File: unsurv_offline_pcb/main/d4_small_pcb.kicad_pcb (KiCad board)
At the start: 4 copper layers, 32 x 45 mm, 61 parts, among them J1 U_FL-R-SMT-1_10_, J2 S2B-PH-SM4-TB_LF__SN_, Q1 UMH3N, U1 TTGO-Micro32-ESP32, U2 RF430CL330HIRGTR‎, U3 CAM-M8C-0-10, U4 AP2112K-3.3, U5 CH340G, U6 BQ25180, U7 BMA400-I2C, U8 RFM95W-868S2

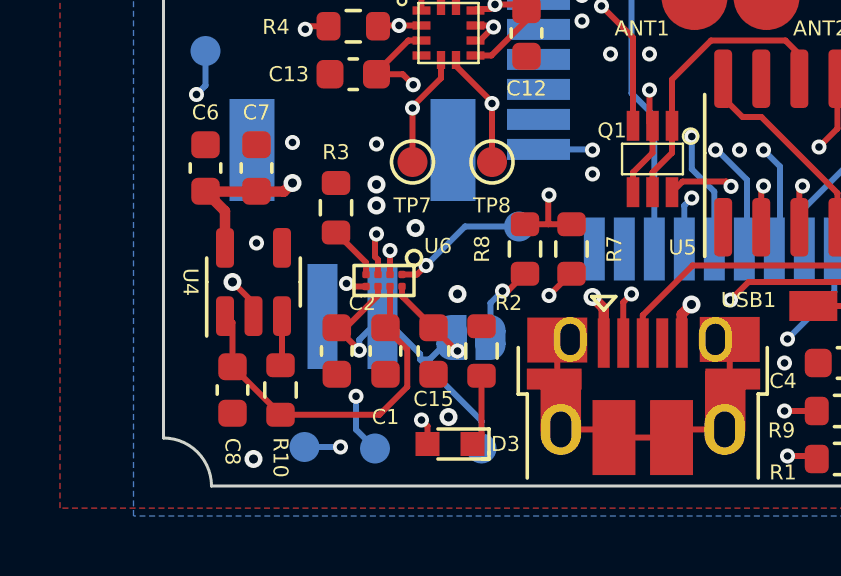
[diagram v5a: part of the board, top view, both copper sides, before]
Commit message: lower clearance for GND fills
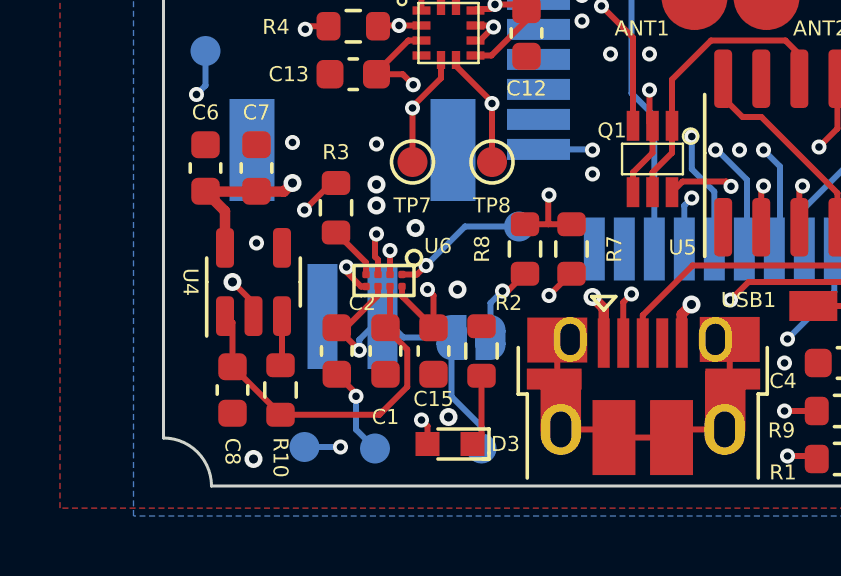
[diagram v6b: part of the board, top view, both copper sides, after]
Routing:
- net GND: track 16.9 -> 19.6 mm, vias 74 -> 75
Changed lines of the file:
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@@
   (segment (start 25.15 58.35) (end 25.15 58.65) (width 0.2) (layer "F.Cu") (net 3))
   (via (at 24.526334 60.475) (size 0.5) (drill 0.25) (layers "F.Cu" "B.Cu") (net 3))
-  (segment (start 26.867721 60.782279) (end 27.6 60.05) (width 0.2) (layer "B.Cu") (net 3))
-  (segment (start 28.6 63.75) (end 28.6 62.827668) (width 0.2) (layer "B.Cu") (net 3))
   (segment (start 24.526334 60.475) (end 24.526334 60.123666) (width 0.2) (layer "B.Cu") (net 3))
   (segment (start 24.526334 60.123666) (end 25.3 59.35) (width 0.2) (layer "B.Cu") (net 3))
-  (segment (start 26.554611 60.782279) (end 26.554611 60.604611) (width 0.2) (layer "B.Cu") (net 3))
-  (segment (start 26.554611 60.782279) (end 26.867721 60.782279) (width 0.2) (layer "B.Cu") (net 3))
-  (segment (start 26.554611 60.604611) (end 25.3 59.35) (width 0.2) (layer "B.Cu") (net 3))
-  (segment (start 28.6 62.827668) (end 26.554611 60.782279) (width 0.2) (layer "B.Cu") (net 3))
+  (segment (start 28.6 63.75) (end 28.6 63.022182) (width 0.2) (layer "B.Cu") (net 3))
+  (segment (start 27.6 60.05) (end 26 60.05) (width 0.2) (layer "B.Cu") (net 3))
+  (segment (start 27.6 62.022182) (end 27.6 60.05) (width 0.2) (layer "B.Cu") (net 3))
+  (segment (start 26 60.05) (end 25.3 59.35) (width 0.2) (layer "B.Cu") (net 3))
+  (segment (start 28.6 63.022182) (end 27.6 62.022182) (width 0.2) (layer "B.Cu") (net 3))
+  (segment (start 24.417052 61.915718) (end 23.776334 61.275) (width 0.2) (layer "F.Cu") (net 4))
   (segment (start 39.7 39.75) (end 39.7 39.056416) (width 0.2) (layer "F.Cu") (net 4))
   (segment (start 31.575 57.925) (end 30.85 58.65) (width 0.2) (layer "F.Cu") (net 4))
+  (segment (start 24.1 57.7) (end 24.1 57.866942) (width 0.2) (layer "F.Cu") (net 4))
   (segment (start 26.6 49.15) (end 26.6 48.5) (width 0.2) (layer "F.Cu") (net 4))
   (segment (start 39 39.05) (end 39.706416 39.05) (width 0.2) (layer "F.Cu") (net 4))
+  (segment (start 23.6 54.9) (end 22.7 55.8) (width 0.2) (layer "F.Cu") (net 4))
   (segment (start 35.9 39.75) (end 36.8 39.75) (width 0.2) (layer "F.Cu") (net 4))
   (segment (start 39.706416 39.05) (end 40.05 39.05) (width 0.2) (layer "F.Cu") (net 4))
+  (segment (start 23.75 54.9) (end 23.6 54.9) (width 0.2) (layer "F.Cu") (net 4))
   (segment (start 35.6 58.949989) (end 35.275 59.274989) (width 0.35) (layer "F.Cu") (net 4))
   (segment (start 40.05 39.05) (end 40.65 38.45) (width 0.2) (layer "F.Cu") (net 4))
@@
   (segment (start 40.65 37.75) (end 39.1 36.2) (width 0.2) (layer "F.Cu") (net 4))
   (segment (start 21 58.9) (end 21 59.3) (width 0.2) (layer "F.Cu") (net 4))
-  (segment (start 24.2 58.35) (end 24.75 58.35) (width 0.2) (layer "F.Cu") (net 4))
   (segment (start 33.25 39.25) (end 33.5875 39.5875) (width 0.2) (layer "F.Cu") (net 4))
-  (segment (start 24.1 58.25) (end 24.2 58.35) (width 0.2) (layer "F.Cu") (net 4))
   (segment (start 29 49.7) (end 28.55 50.15) (width 0.2) (layer "F.Cu") (net 4))
   (segment (start 20.3 58.2) (end 21 58.9) (width 0.2) (layer "F.Cu") (net 4))
@@
   (segment (start 28.55 50.15) (end 28.4 50.15) (width 0.2) (layer "F.Cu") (net 4))
   (segment (start 35.275 59.274989) (end 35.275 60.235) (width 0.35) (layer "F.Cu") (net 4))
+  (segment (start 24.583058 58.35) (end 24.75 58.35) (width 0.2) (layer "F.Cu") (net 4))
   (segment (start 29 49.7) (end 28.95 49.65) (width 0.2) (layer "F.Cu") (net 4))
+  (segment (start 24.1 57.866942) (end 24.583058 58.35) (width 0.2) (layer "F.Cu") (net 4))
+  (segment (start 24.417052 62.009055) (end 24.417052 61.915718) (width 0.2) (layer "F.Cu") (net 4))
   (via (at 46 60.1) (size 0.5) (drill 0.25) (layers "F.Cu" "B.Cu") (net 4))
   (via (at 39.9 46.9) (size 0.5) (drill 0.25) (layers "F.Cu" "B.Cu") (net 4))
@@
   (via (at 48.5 23.9) (size 0.5) (drill 0.25) (layers "F.Cu" "B.Cu") (net 4))
   (via (at 19.4 30.4) (size 0.5) (drill 0.25) (layers "F.Cu" "B.Cu") (net 4))
+  (via (at 22.7 55.8) (size 0.5) (drill 0.25) (layers "F.Cu" "B.Cu") (net 4))
   (via (at 44.1 32.7) (size 0.5) (drill 0.25) (layers "F.Cu" "B.Cu") (net 4))
   (via (at 27.5 30.4) (size 0.5) (drill 0.25) (layers "F.Cu" "B.Cu") (net 4))
@@
   (via (at 35.5 30.4) (size 0.5) (drill 0.25) (layers "F.Cu" "B.Cu") (net 4))
   (via (at 35.1 23.2) (size 0.5) (drill 0.25) (layers "F.Cu" "B.Cu") (net 4))
-  (via (at 24.1 58.25) (size 0.5) (drill 0.25) (layers "F.Cu" "B.Cu") (net 4))
+  (via (at 24.1 57.7) (size 0.5) (drill 0.25) (layers "F.Cu" "B.Cu") (net 4))
   (via (at 29 49.7) (size 0.5) (drill 0.25) (layers "F.Cu" "B.Cu") (net 4))
   (via (at 21.5 30.7) (size 0.5) (drill 0.25) (layers "F.Cu" "B.Cu") (net 4))
@@
   (via (at 44 29.5) (size 0.5) (drill 0.25) (layers "F.Cu" "B.Cu") (net 4))
   (via (at 27.5 42.4) (size 0.5) (drill 0.25) (layers "F.Cu" "B.Cu") (net 4))
-  (via (at 27.8 58.6) (size 0.6) (drill 0.3) (layers "F.Cu" "B.Cu") (net 4))
+  (via (at 27.8 58.45) (size 0.6) (drill 0.3) (layers "F.Cu" "B.Cu") (net 4))
   (via (at 44.1 23.3) (size 0.5) (drill 0.25) (layers "F.Cu" "B.Cu") (net 4))
   (via (at 35.4 39.25) (size 0.5) (drill 0.25) (layers "F.Cu" "B.Cu") (net 4))
@@
   (segment (start 26.8 63) (end 26.6 62.8) (width 0.2) (layer "F.Cu") (net 5))
   (segment (start 32.3 58.7) (end 32.675 59.075) (width 0.35) (layer "F.Cu") (net 5))
-  (segment (start 27.775 60.5) (end 27 59.725) (width 0.2) (layer "F.Cu") (net 5))
-  (segment (start 27.8 60.5) (end 27.775 60.5) (width 0.2) (layer "F.Cu") (net 5))
+  (segment (start 27 58.65) (end 27 59.725) (width 0.2) (layer "F.Cu") (net 5))
+  (segment (start 26.8 58.45) (end 27 58.65) (width 0.2) (layer "F.Cu") (net 5))
   (segment (start 25.95 58.35) (end 25.95 58.675) (width 0.2) (layer "F.Cu") (net 5))
   (via (at 23.9 63.7) (size 0.5) (drill 0.25) (layers "F.Cu" "B.Cu") (net 5))
   (via (at 26.6 62.8) (size 0.5) (drill 0.25) (layers "F.Cu" "B.Cu") (net 5))
-  (via (at 27.8 60.5) (size 0.5) (drill 0.25) (layers "F.Cu" "B.Cu") (net 5))
+  (via (at 26.8 58.45) (size 0.5) (drill 0.25) (layers "F.Cu" "B.Cu") (net 5))
   (via (at 32.3 58.7) (size 0.6) (drill 0.3) (layers "F.Cu" "B.Cu") (net 5))
   (segment (start 23.9 63.7) (end 22.7 63.7) (width 0.2) (layer "B.Cu") (net 5))
@@
   (segment (start 41.1 21.7) (end 41.1 23.3) (width 0.2) (layer "B.Cu") (net 91))
   (zone (net 4) (net_name "GND") (layer "F.Cu") (hatch edge 0.508)
-    (connect_pads (clearance 0.2))
+    (connect_pads (clearance 0.15))
     (min_thickness 0.254) (filled_areas_thickness no)
     (fill yes (thermal_gap 0.508) (thermal_bridge_width 0.508))
@@
   )
   (zone (net 4) (net_name "GND") (layer "B.Cu") (hatch edge 0.508)
-    (connect_pads (clearance 0.3))
+    (connect_pads (clearance 0.15))
     (min_thickness 0.254) (filled_areas_thickness no)
     (fill yes (thermal_gap 0.508) (thermal_bridge_width 0.508))

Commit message: pre-production run
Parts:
- removed D3: LED, digikey-footprints:LED_0603
- removed R2: 1k, Resistor_SMD:R_0603_1608Metric
- U2: footprint unsurv_offline_pcb_footprints:RF430_3x3mm -> unsurv_offline_pcb_footprints:RF430_3x3mm_regular
- U7: footprint unsurv_offline_pcb_footprints:BMA400 -> unsurv_offline_pcb_footprints:BMA400_regular
- turned U7 to -90 degrees
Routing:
- net Net-(D3-Pad1): track 2.40 -> 0.00 mm
- net GND: track 19.6 -> 21.5 mm, vias 75 -> 76
- net +5V: track 6.94 -> 6.06 mm, vias 4 -> 3

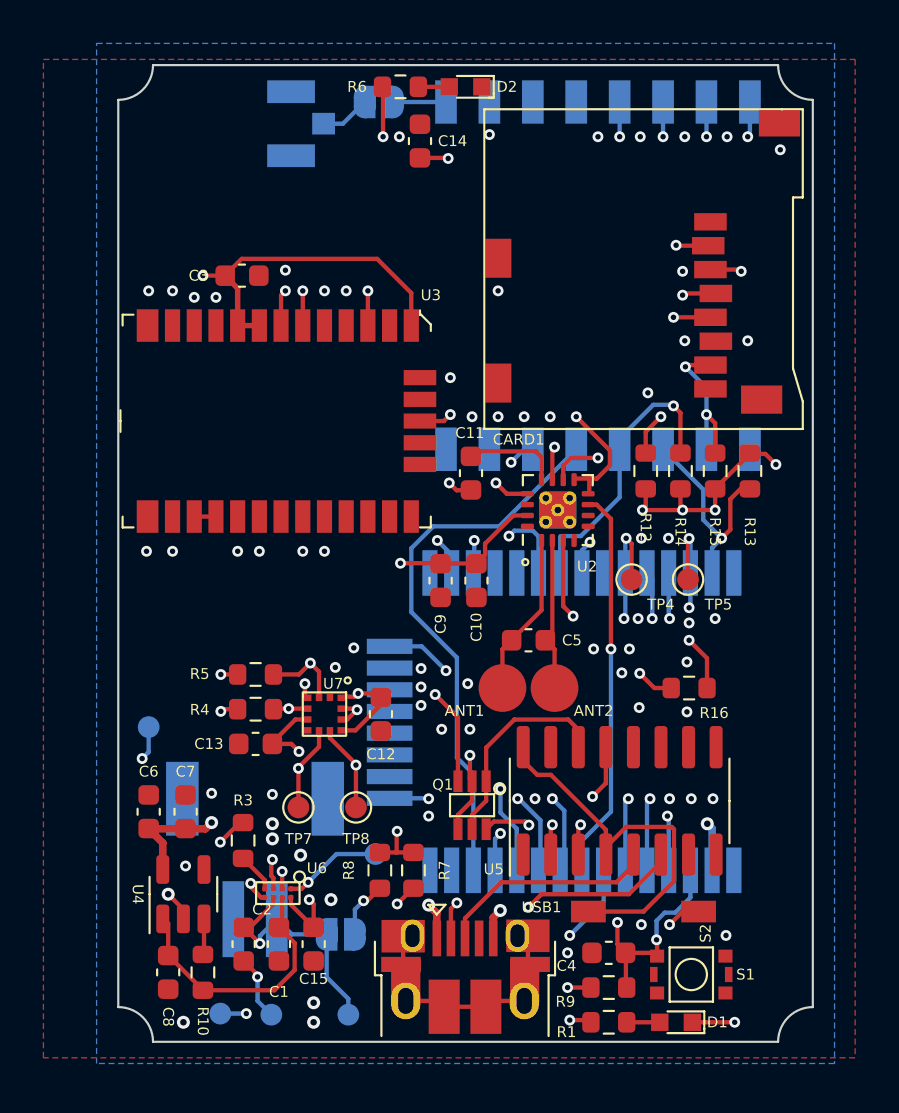
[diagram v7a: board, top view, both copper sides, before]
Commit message: remove hand soldering footprints
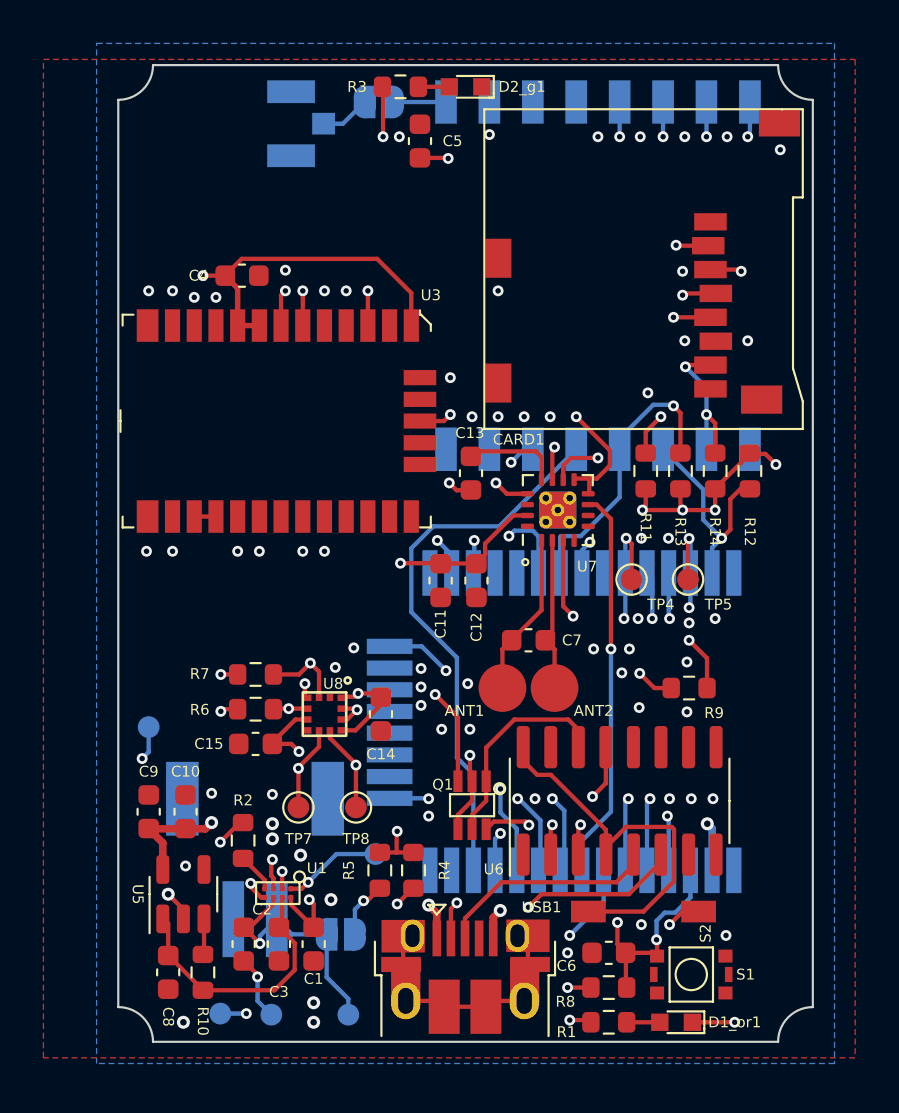
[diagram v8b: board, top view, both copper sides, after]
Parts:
- removed the U7 at (27.5, 49.9)
- added U8: BMA400, unsurv_offline_pcb_footprints:BMA400_regular, F.Cu at (27.5, 49.9)
- C1: renamed from C15; value 1yF -> 1µF
- C10: renamed from C7; value 10yF -> 10µF
- C11: renamed from C9; value 0.1yF -> 0.1µF
- C12: renamed from C10; value 1yF -> 1µF
- C2, C8: value 1yF -> 1µF
- C3: renamed from C1; value 10yF -> 10µF
- C4: renamed from C3; value 4.7yF -> 4.7µF
- C5: renamed from C14; value 4.7yF -> 4.7µF
- C9: renamed from C6; value 1yF -> 1µF
- U3: value CAM-M8C-0-10 -> CAM-M8C
- renumbered C11 to C13, C12 to C14, C13 to C15, C4 to C6, C5 to C7, D1 to D1_or1, D2 to D2_g1, J2 to J1, J1 to J2, R12 to R11, R13 to R12, R14 to R13, R15 to R14, R3 to R2, R6 to R3, R7 to R4, R8 to R5, R4 to R6, R5 to R7, R9 to R8, R16 to R9, U6 to U1, U1 to U2, U8 to U4, U4 to U5, U5 to U6, U2 to U7
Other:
- board text added: "unsurv offline v0.5 pre production"
- board text removed: "unsurv offline v0.4 pre production"
